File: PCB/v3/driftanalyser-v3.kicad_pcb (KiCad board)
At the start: 4 copper layers, 55 x 100 mm, 172 parts, among them J1 6437288-1, J2 Stud_M6, J3 USB-C 16P, J4 UART0, Q1 BSC016N06NS, Q2 BSC016N06NS, SW1 BOOT, SW2 EN, U1 ESP32-S3-WROOM-1U-N16R2, U10 BTS7008-2EPA, U11 BTS7008-2EPA, U12 BTS7008-2EPA, U13 BTS7008-2EPA, U14 PCA9555PW, U15 74HCT245PW, U16 74HCT245PW, U2 LM74700-Q1, U3 LSM6DS3TR-C, U4 TJA1051T/3, U5 TJA1027T/20, U6 TPS2553DBV, U7 LMR36520ADDAR, U8 AP7361C-33E, U9 USBLC6-2SC6

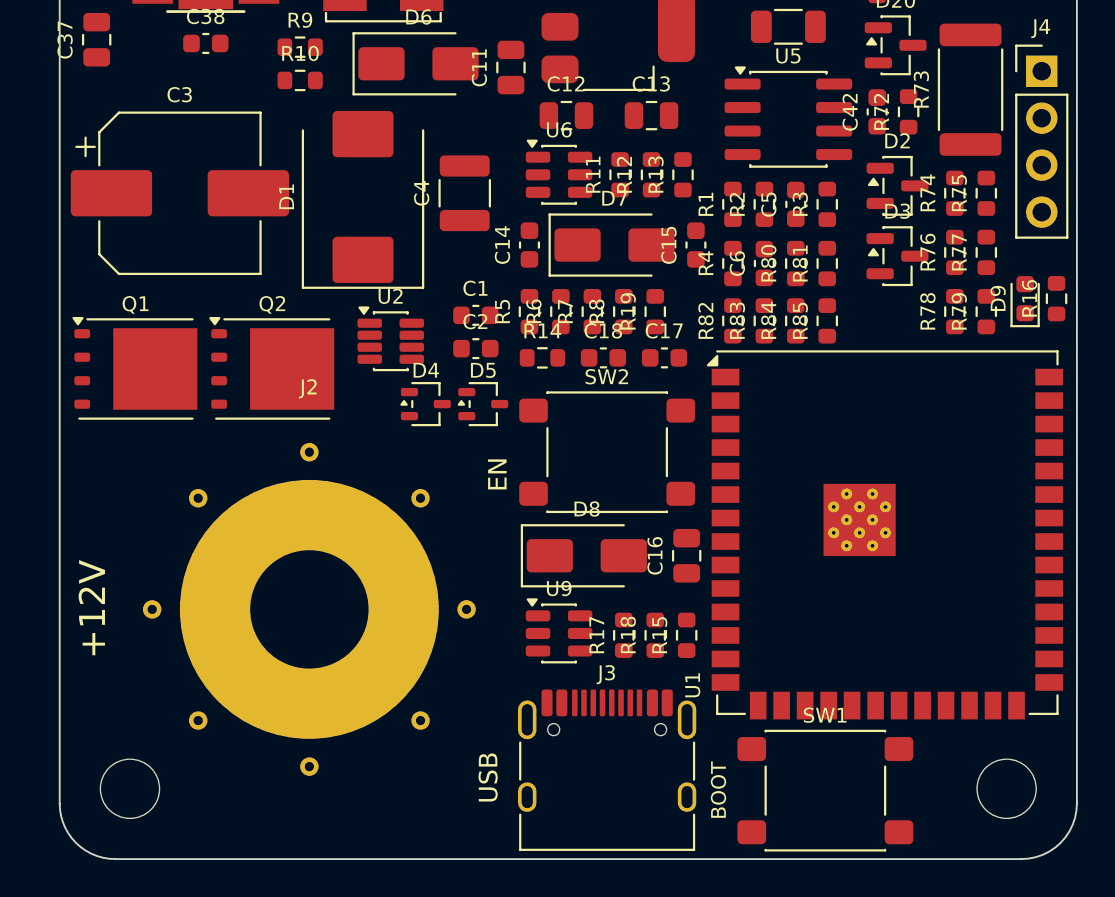
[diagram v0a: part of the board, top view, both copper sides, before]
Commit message: pcb v3: power path order, imu axes
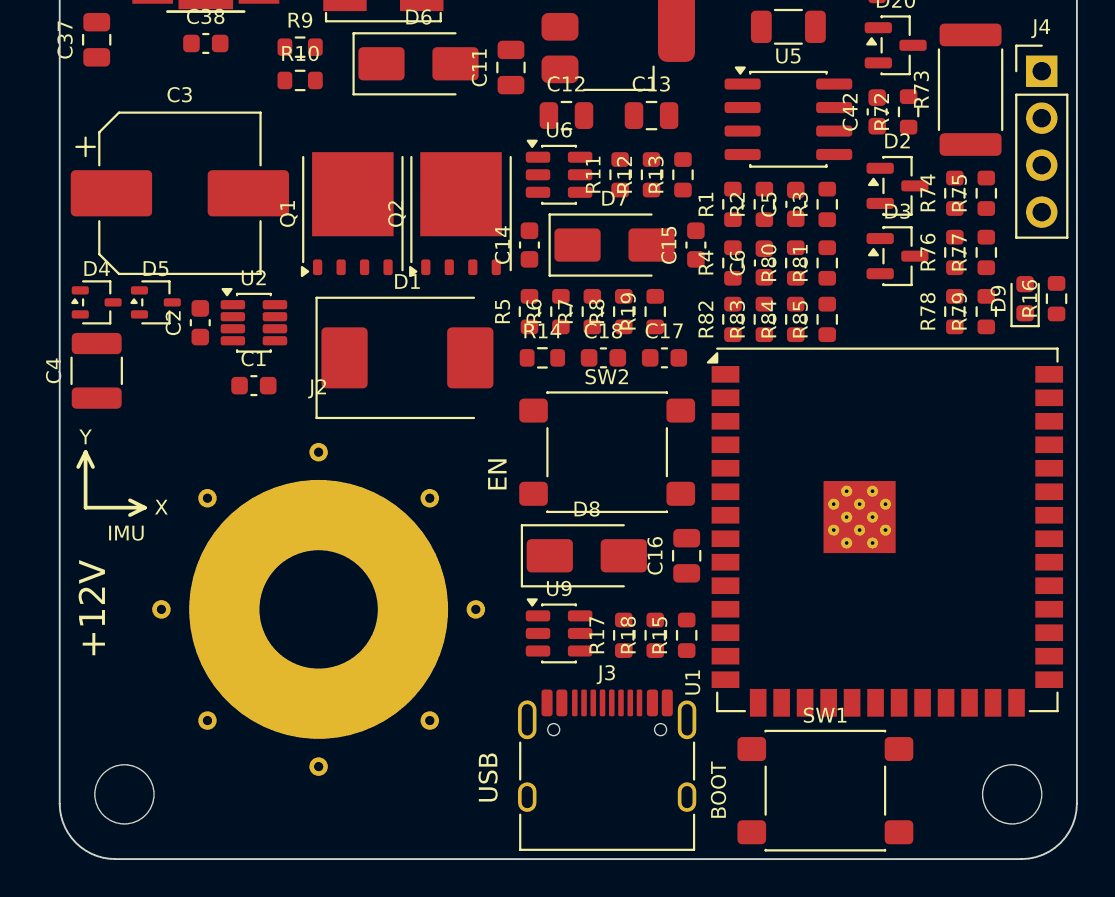
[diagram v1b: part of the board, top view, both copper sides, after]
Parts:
- moved C4 22.1 mm to (2.00, 73.6)
- moved D4 18.6 mm to (2.00, 69.9)
- moved D5 18.5 mm to (5.20, 69.9)
- moved C2 15.0 mm to (7.60, 71.0), turned to 90 degrees
- moved Q1 14.4 mm to (15.8, 65.1), turned to 90 degrees
- moved Q2 13.2 mm to (21.7, 65.1), turned to 90 degrees
- moved C1 12.6 mm to (10.5, 74.4)
- moved D1 9.02 mm to (18.8, 72.9), turned to 0 degrees
- moved U2 7.47 mm to (10.5, 71.0)
- moved J2 0.50 mm to (14.0, 86.5)
- moved H3 0.42 mm to (3.50, 96.5)
- moved H4 0.42 mm to (51.5, 96.5)
- moved U1 0.15 mm to (44.8, 82.2)
- moved R82 0.08 mm to (36.4, 70.8)
- moved R83 0.08 mm to (38.1, 70.8)
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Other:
- board text added: "IMU"
- board text added: "X"
- board text added: "Y"

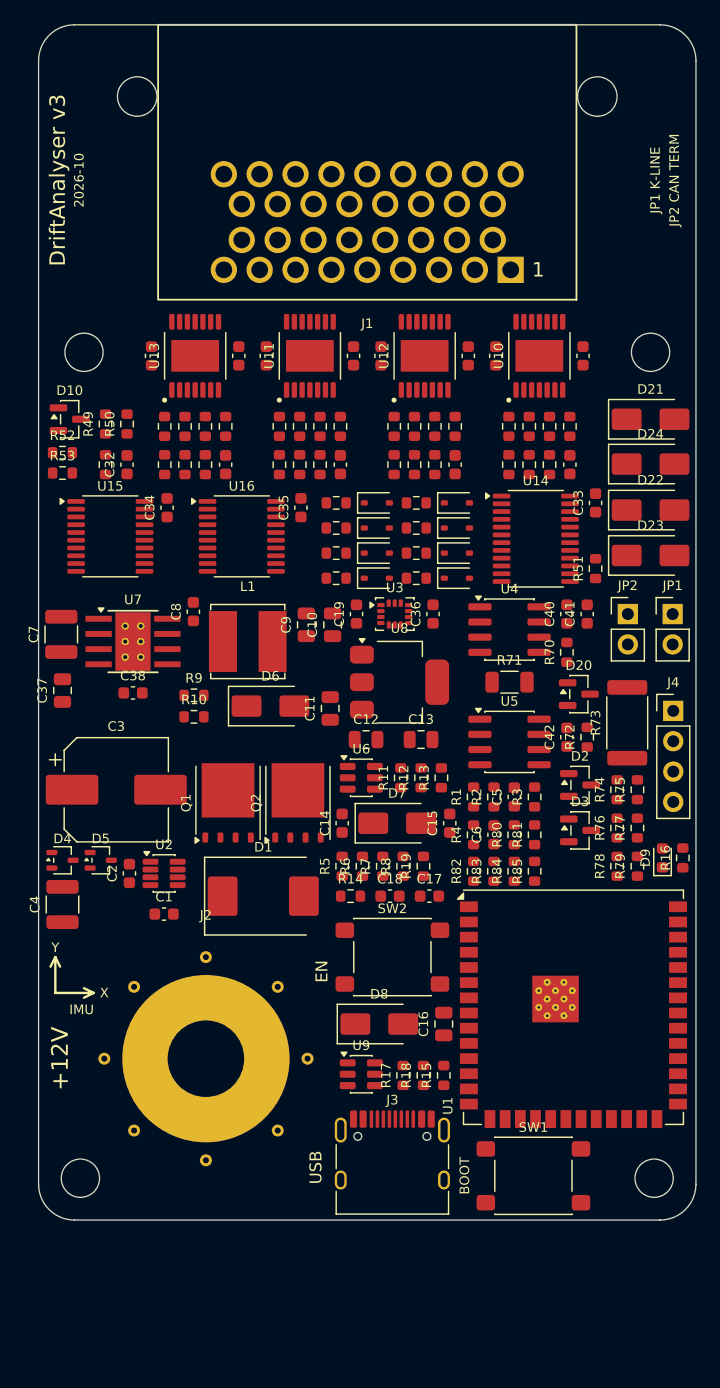
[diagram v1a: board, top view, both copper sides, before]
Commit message: pcb v3: power copper, routed, 25 open
led pours into j1 row 1, vin/vbus planes, ties, freerouting on tengri, session replayed
drc not clean yet: 25 unconnected, 9 errors

Claude-Session: https://claude.ai/code/session_01MELKvCtSrN4XHin3AfxGm6
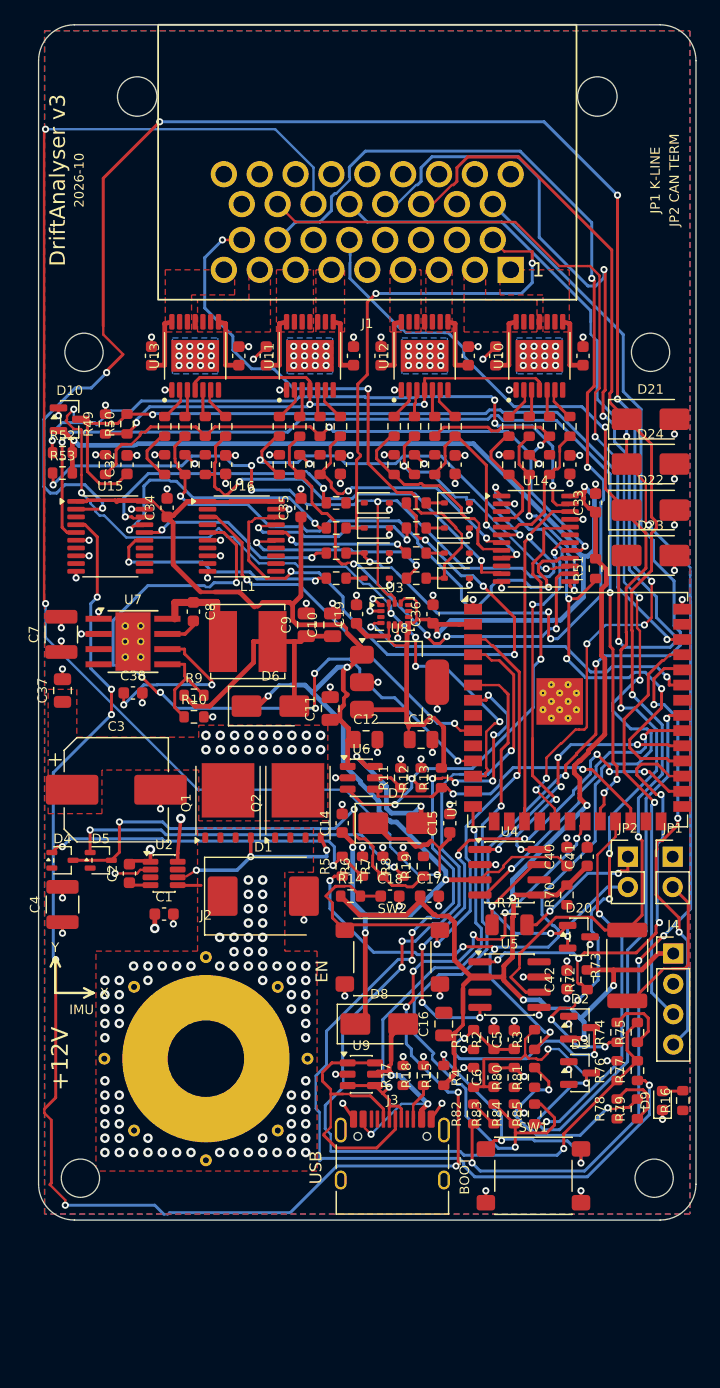
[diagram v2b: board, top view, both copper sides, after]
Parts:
- moved U1 24.9 mm to (45.1, 57.3)
- moved C5 20.3 mm to (39.8, 84.9)
- moved R1 20.3 mm to (36.4, 84.9)
- moved R2 20.3 mm to (38.1, 84.9)
- moved R3 20.3 mm to (41.5, 84.9)
- moved R82 20.3 mm to (36.4, 91.1)
- moved R83 20.3 mm to (38.1, 91.1)
- moved R84 20.3 mm to (39.8, 91.1)
- moved R85 20.3 mm to (41.5, 91.1)
- moved C42 20.3 mm to (44.2, 79.9)
- moved D2 20.3 mm to (45.3, 83.9)
- moved J4 20.3 mm to (53.1, 77.7)
- moved R72 20.3 mm to (45.9, 79.9)
- moved R73 20.3 mm to (49.2, 78.7)
- moved U4 20.3 mm to (39.4, 70.9)
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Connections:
- J1 pad 1: LED1_12V -> LED2_12V
- J1 pad 10: LED4_12V -> LED2_DO
- J1 pad 11: LED4_DO -> LED1_DO
- J1 pad 12: GND -> LED6_DO
- J1 pad 13: LED5_12V -> LED5_DO
- J1 pad 14: LED5_DO -> IN1
- J1 pad 15: GND -> LED4_DO
- J1 pad 16: CANH -> LED3_DO
- J1 pad 17: CANL -> LED8_DO
- J1 pad 18: KLINE -> CANH
- J1 pad 19: IGN -> CANL
- J1 pad 2: LED1_DO -> LED1_12V
- J1 pad 20: GND -> KLINE
- J1 pad 21: 5V_SENS -> IN2
- J1 pad 22: IN1 -> IN3
- J1 pad 23: IN2 -> 5V_SENS
- J1 pad 24: GND -> IGN
- J1 pad 25: IN3 -> LED7_DO
- J1 pad 26: LED6_12V -> GND
- J1 pad 27: LED6_DO -> GND
- J1 pad 29: LED7_12V -> GND
- J1 pad 3: GND -> LED6_12V
- J1 pad 30: LED7_DO -> GND
- J1 pad 32: LED8_12V -> GND
- J1 pad 33: LED8_DO -> GND
- J1 pad 4: LED2_12V -> LED5_12V
- J1 pad 5: LED2_DO -> GND
- J1 pad 6: GND -> LED4_12V
- J1 pad 8: LED3_DO -> LED8_12V
- J1 pad 9: GND -> LED7_12V
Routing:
- net 3V3: track 0.00 -> 221.8 mm, vias 0 -> 8
- net LED1_DATA: track 0.00 -> 147.1 mm, vias 0 -> 10
- net LED3_DATA: track 0.00 -> 138.3 mm, vias 0 -> 12
- net IGN: track 0.00 -> 132.3 mm, vias 0 -> 7
- net 5V: track 0.00 -> 129.9 mm, vias 0 -> 5
- net 5V_SENS: track 0.00 -> 121.9 mm, vias 0 -> 3
- net I2C_SDA: track 0.00 -> 116.5 mm, vias 0 -> 10
- net IN3: track 0.00 -> 116.2 mm, vias 0 -> 5
- net GND: track 0.00 -> 105.2 mm, vias 0 -> 112
- net KLINE: track 0.00 -> 99.3 mm, vias 0 -> 2
- net IN1: track 0.00 -> 95.6 mm, vias 0 -> 7
- net LED3_DO: track 0.00 -> 92.8 mm, vias 0 -> 5
- net I2C_SCL: track 0.00 -> 91.2 mm, vias 0 -> 5
- net CANH: track 0.00 -> 90.2 mm, vias 0 -> 4
- net IN1_PULL: track 0.00 -> 88.7 mm, vias 0 -> 8
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- added copper zone on B.Cu, net GND
- added copper zone on F.Cu, net GND
- added copper zone on In1.Cu, net GND
- added copper zone on In2.Cu, net GND
- added copper zone on F.Cu, net LED1_12V
- added copper zone on F.Cu, net LED2_12V
- added copper zone on F.Cu, net LED3_12V
- added copper zone on F.Cu, net LED4_12V
- added copper zone on F.Cu, net LED5_12V
- added copper zone on F.Cu, net LED6_12V
- added copper zone on F.Cu, net LED7_12V
- added copper zone on F.Cu, net LED8_12V
- added copper zone on B.Cu, net VBUS
- added copper zone on F.Cu, net VBUS
- added copper zone on In2.Cu, net VBUS
- added copper zone on F.Cu, net VIN
- added copper zone on In2.Cu, net VIN

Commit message: pcb v3: 6 layers, routed, drc clean
jlc06161h-3313 1oz inner, signals on in2/in4, power planes on in3 + outer led lanes, 3 links by hand

Claude-Session: https://claude.ai/code/session_01MELKvCtSrN4XHin3AfxGm6
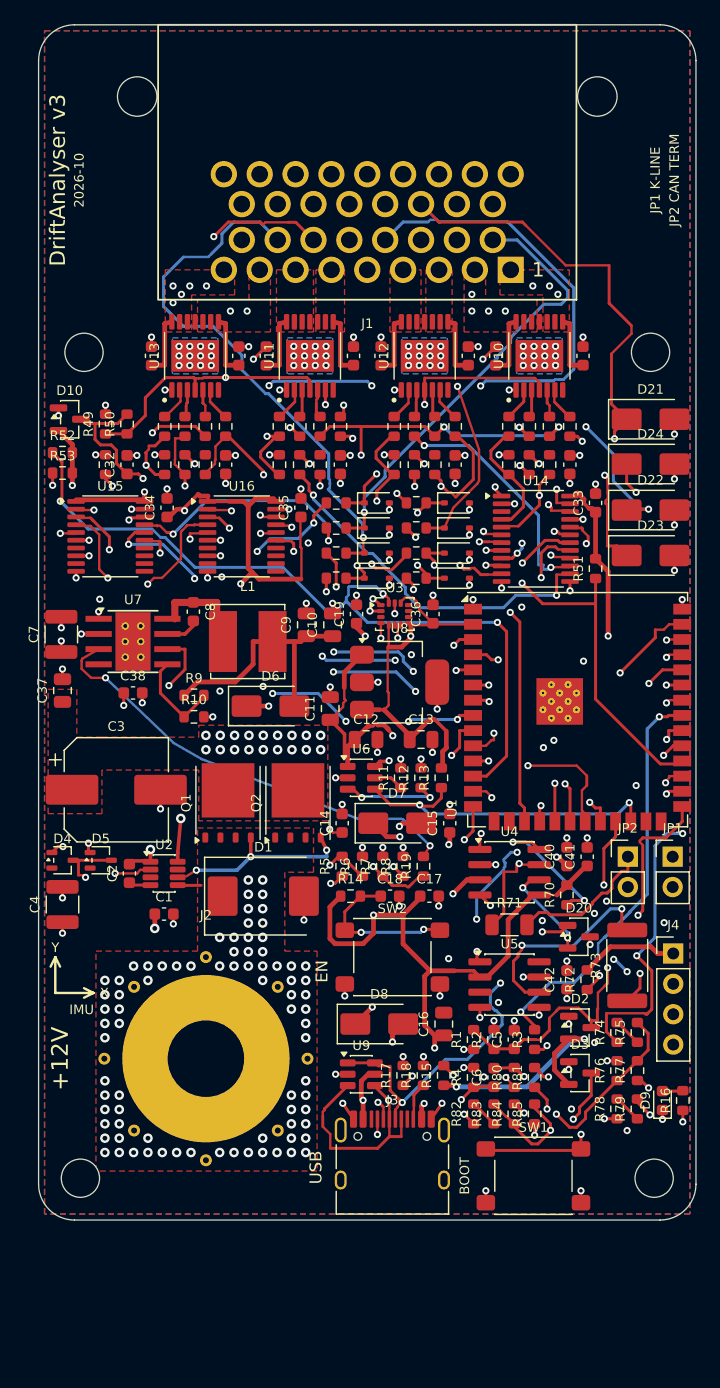
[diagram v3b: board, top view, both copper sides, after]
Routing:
- net LED1_DATA: track 147.1 -> 57.0 mm, vias 10 -> 5
- net CANL: track 8.20 -> 91.0 mm, vias 1 -> 2
- net LED3_DATA: track 138.3 -> 57.3 mm, vias 12 -> 2
- net STATUS_LED: track 0.00 -> 72.2 mm, vias 0 -> 6
- net LED7_DO: track 1.53 -> 56.4 mm, vias 0 -> 3
- net LED2_DATA: track 0.00 -> 54.9 mm, vias 0 -> 4
- net LED4_DO: track 1.52 -> 51.1 mm, vias 0 -> 2
- net LED5_DO: track 1.53 -> 49.5 mm, vias 0 -> 2
- net LED3_DO: track 92.8 -> 45.9 mm, vias 5 -> 1
- net LED7_DATA: track 0.00 -> 45.1 mm, vias 0 -> 2
- net IN1_PULL: track 88.7 -> 46.8 mm, vias 8 -> 6
- net IN2_SENSE: track 18.5 -> 59.5 mm, vias 2 -> 5
- net LED1_DO: track 0.00 -> 39.4 mm, vias 0 -> 1
- net BOOT: track 20.9 -> 59.2 mm
- net IN2: track 75.4 -> 112.8 mm, vias 3 -> 2
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- added copper zone on In3.Cu, net GND
- added copper zone on In4.Cu, net GND
- added copper zone on In3.Cu, net LED1_12V
- added copper zone on In3.Cu, net LED2_12V
- added copper zone on In3.Cu, net LED7_12V
- added copper zone on In3.Cu, net LED8_12V
- added copper zone on In3.Cu, net VBUS
- added copper zone on In3.Cu, net VIN
- removed copper zone on In2.Cu, net VBUS
- removed copper zone on In2.Cu, net VIN
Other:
- copper layers 4 -> 6

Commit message: pcb v3: gnd stud j5, board 55x112 (placement only)
doesnt fit in 100, unrouted, needs author ok on the size
Claude-Session: https://claude.ai/code/session_01MELKvCtSrN4XHin3AfxGm6
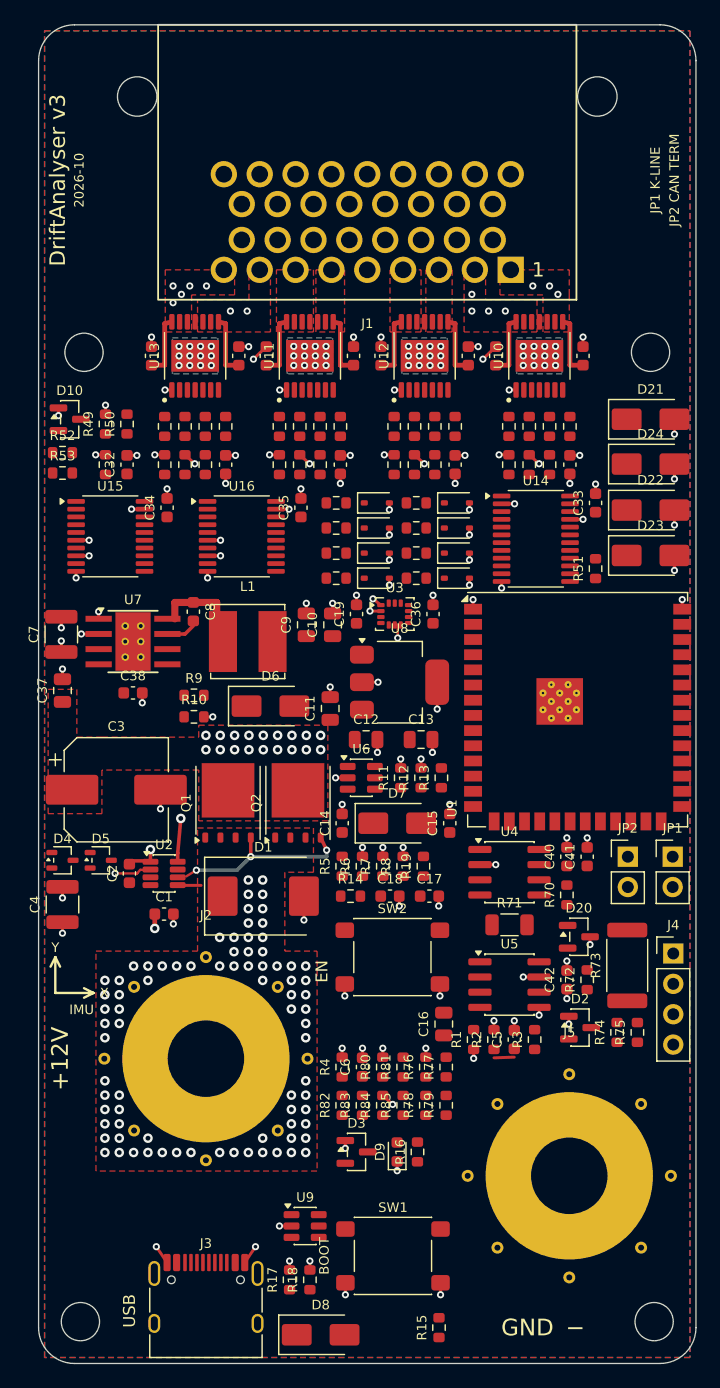
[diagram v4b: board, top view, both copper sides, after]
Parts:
- added J5: Stud_M6, da3:Stud_M6, F.Cu at (44.4, 96.3)
- moved D8 26.5 mm to (23.6, 109.6)
- moved D9 22.6 mm to (30.0, 94.3)
- moved R16 22.6 mm to (31.7, 94.3)
- moved R15 21.1 mm to (33.5, 109.0)
- moved D3 19.8 mm to (26.6, 94.3)
- moved J3 19.7 mm to (14.0, 107.6)
- moved R18 19.6 mm to (22.7, 105.0)
- moved R17 19.6 mm to (21.0, 105.0)
- moved R76 16.0 mm to (32.4, 87.2)
- moved R77 16.0 mm to (34.1, 87.2)
- moved R78 16.0 mm to (32.4, 90.4)
- moved R79 16.0 mm to (34.1, 90.4)
- moved U9 13.5 mm to (22.3, 100.5)
- moved SW1 13.5 mm to (29.6, 103.0)
- moved H3 12.0 mm to (3.50, 108.5)
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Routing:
- net 3V3: track 219.1 -> 0.00 mm, vias 8 -> 0
- net 5V: track 133.3 -> 0.00 mm, vias 9 -> 0
- net 5V_SENS: track 117.5 -> 0.00 mm, vias 2 -> 0
- net IN3: track 117.3 -> 0.00 mm, vias 4 -> 0
- net IN2: track 112.8 -> 0.00 mm, vias 2 -> 0
- net IGN: track 98.9 -> 0.00 mm, vias 2 -> 0
- net IN1: track 97.7 -> 0.00 mm, vias 4 -> 0
- net KLINE: track 93.3 -> 0.00 mm, vias 3 -> 0
- net I2C_SCL: track 92.4 -> 0.00 mm, vias 4 -> 0
- net CANL: track 91.0 -> 0.00 mm, vias 2 -> 0
- net I2C_SDA: track 87.4 -> 0.00 mm, vias 4 -> 0
- net DSEL: track 81.8 -> 0.00 mm, vias 6 -> 0
- net CANH: track 79.1 -> 0.00 mm, vias 2 -> 0
- net STATUS_LED: track 72.2 -> 0.00 mm, vias 6 -> 0
- net IGN_DET: track 70.8 -> 0.00 mm, vias 4 -> 0
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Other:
- board size 55 x 100 mm -> 55 x 112 mm
- board text added: "GND"
- board text added: "−"

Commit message: pcb v3: 55x112 routed, drc clean
tengri p30 (= o30), 7 fr-unrouted -> 1 kicad link, buck_en by hand
Claude-Session: https://claude.ai/code/session_01MELKvCtSrN4XHin3AfxGm6
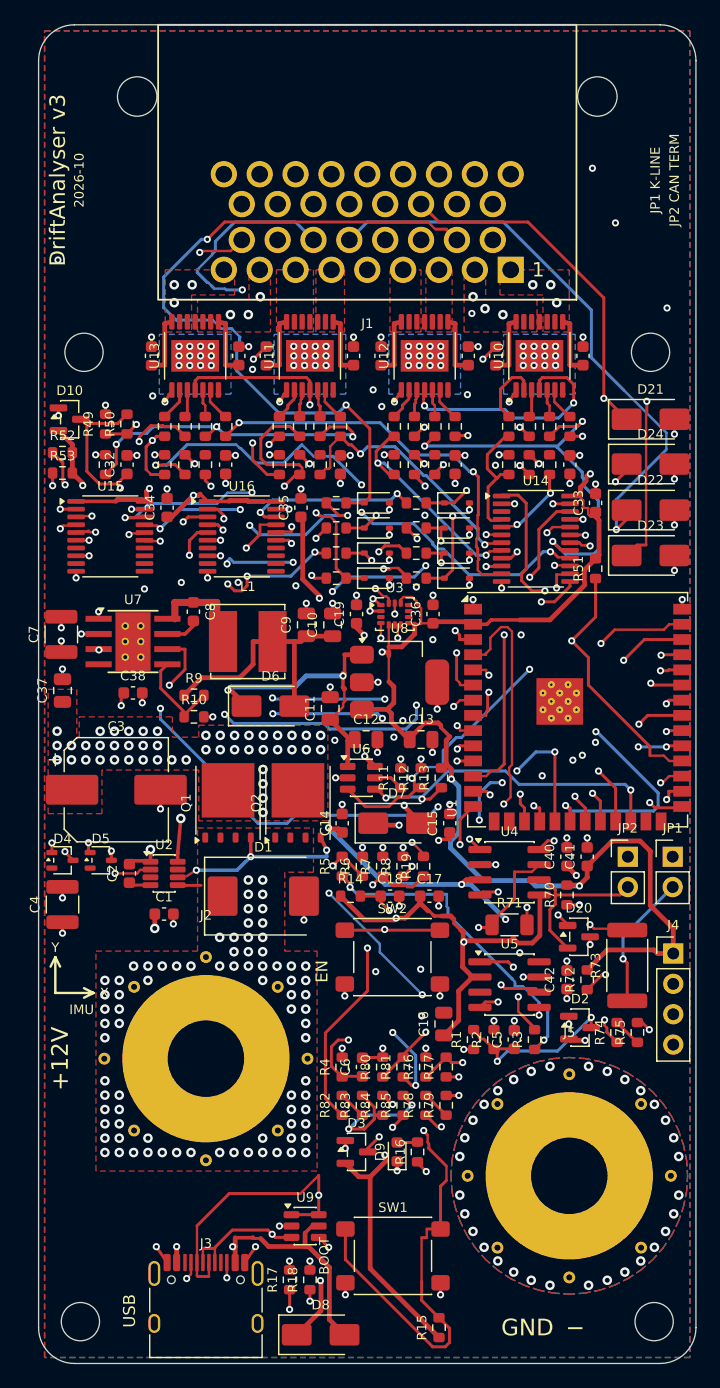
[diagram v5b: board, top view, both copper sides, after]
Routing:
- net 3V3: track 0.00 -> 309.7 mm, vias 0 -> 12
- net 5V: track 0.00 -> 165.1 mm, vias 0 -> 10
- net IN2: track 0.00 -> 135.0 mm, vias 0 -> 2
- net IN3: track 0.00 -> 122.5 mm, vias 0 -> 4
- net IGN: track 0.00 -> 103.1 mm, vias 0 -> 2
- net 5V_SENS: track 0.00 -> 101.4 mm, vias 0 -> 3
- net KLINE: track 0.00 -> 97.1 mm, vias 0 -> 4
- net IN1: track 0.00 -> 93.5 mm, vias 0 -> 2
- net CANL: track 0.00 -> 92.8 mm, vias 0 -> 1
- net CANH: track 0.00 -> 84.3 mm, vias 0 -> 2
- net BOOT: track 0.00 -> 83.2 mm, vias 0 -> 2
- net I2C_SCL: track 0.00 -> 80.4 mm, vias 0 -> 4
- net I2C_SDA: track 0.00 -> 77.4 mm, vias 0 -> 4
- net IGN_DET: track 0.00 -> 76.6 mm, vias 0 -> 5
- net LED2_DATA: track 0.00 -> 70.2 mm, vias 0 -> 5
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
